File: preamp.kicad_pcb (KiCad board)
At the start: 2 copper layers, 70 x 67 mm, 69 parts, among them J1 AC, J2 JST_XH_3, J3 JST_XH_3, J4 JST_XH_3, J6 JST_XH_3, SW1 SW_SPST, SW2 SW_SPST, U1 L78L09_SOT89, U2 L78L05_SOT89, U3 NJM2753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

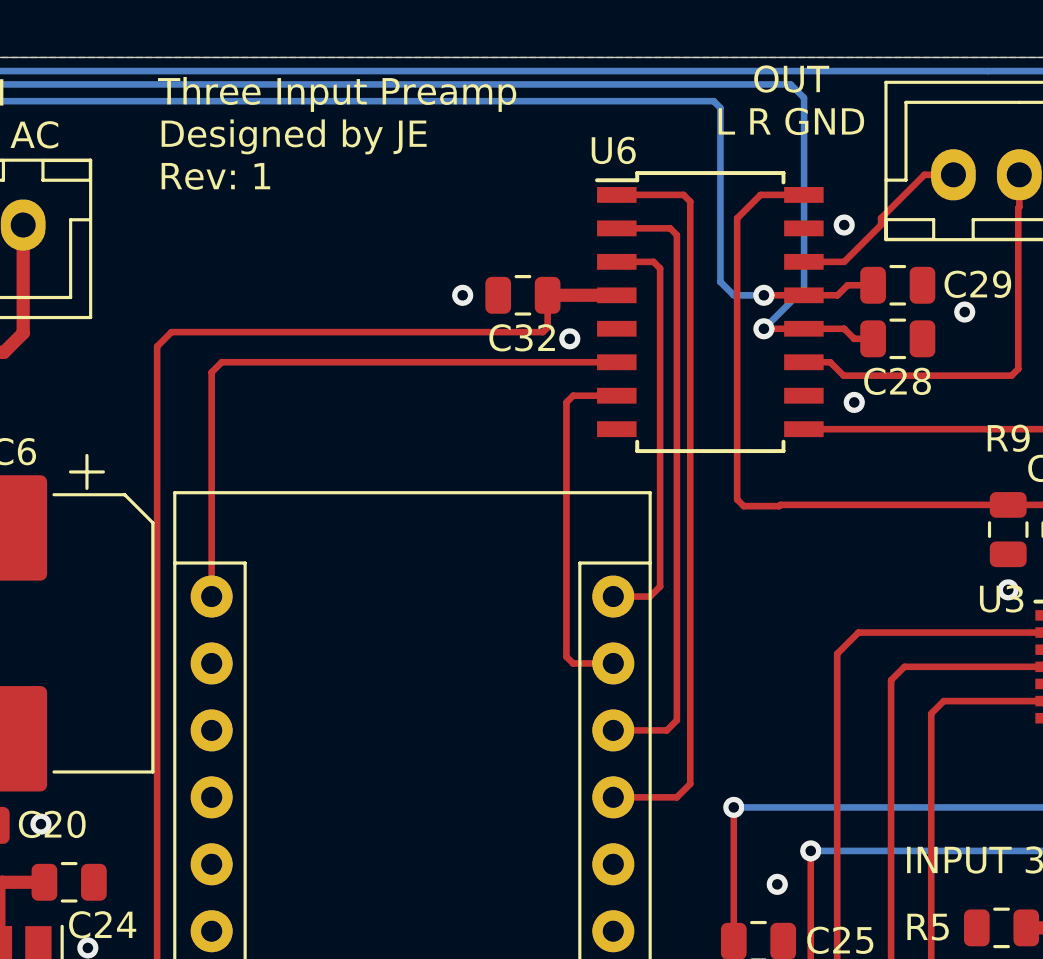
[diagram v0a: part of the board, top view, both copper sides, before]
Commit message: prototype built, tested and installed into hifi system
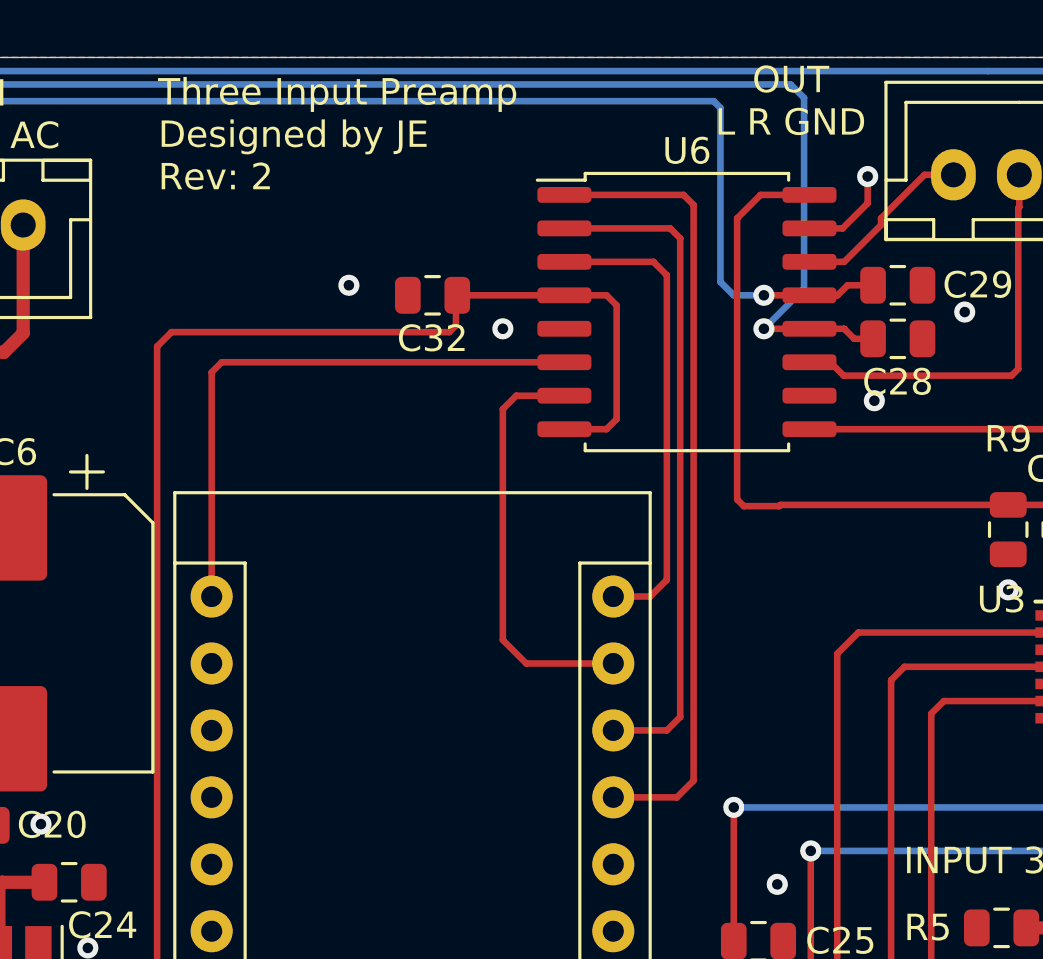
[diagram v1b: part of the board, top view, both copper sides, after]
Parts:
- U6: footprint Package_SO:SOIC-16W_5.3x10.2mm_P1.27mm -> Package_SO:SOIC-16W_7.5x10.3mm_P1.27mm
- moved C32 3.43 mm to (99.8, 81.0)
- moved U6 0.89 mm to (109.5, 81.7)
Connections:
- U6 pad 8: Net-(U6-Pad8) -> +5VD
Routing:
- net +5VD: track 115.3 -> 121.8 mm
- net GND: track 1.42 -> 5.04 mm
- net /MISO: track 13.6 -> 15.9 mm
- net /MOSI: track 15.8 -> 18.0 mm
- net /ZCEN: track 28.1 -> 30.2 mm
- net /CS: track 23.4 -> 25.5 mm
- net /SCLK: track 24.0 -> 22.1 mm
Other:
- board text added: "Three Input Preamp Designed by JE Rev: 2"
- board text removed: "Three Input Preamp Designed by JE Rev: 1"
